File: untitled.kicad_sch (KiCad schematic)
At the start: 12 parts, among them U4 LM2596S-5, U5 LM2596S-12

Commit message: add last footprints
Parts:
- C1, C6: value CP -> 470uF; footprint Capacitor_THT:CP_Radial_D10.0mm_P5.00mm -> Capacitor_THT:CP_Radial_D12.5mm_P5.00mm
- C2, C7: value CP -> 220uF
- L1, L2, L3, L4: value L -> 10uH
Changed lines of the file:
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@@
       (effects (font (size 1.27 1.27)) (justify left))
     )
-    (property "Value" "CP" (id 1) (at 58.8772 54.483 0)
-      (effects (font (size 1.27 1.27)) (justify left))
-    )
-    (property "Footprint" "Capacitor_THT:CP_Radial_D10.0mm_P5.00mm" (id 2) (at 56.8452 57.15 0)
+    (property "Value" "470uF" (id 1) (at 58.8772 54.483 0)
+      (effects (font (size 1.27 1.27)) (justify left))
+    )
+    (property "Footprint" "Capacitor_THT:CP_Radial_D12.5mm_P5.00mm" (id 2) (at 56.8452 57.15 0)
       (effects (font (size 1.27 1.27)) hide)
     )
@@
     (in_bom yes) (on_board yes)
     (property "Reference" "L3" (id 0) (at 129.54 42.3926 90))
-    (property "Value" "L" (id 1) (at 129.54 44.704 90))
+    (property "Value" "10uH" (id 1) (at 129.54 44.704 90))
     (property "Footprint" "Inductor_SMD:L_TDK_SLF10145" (id 2) (at 129.54 46.99 0)
       (effects (font (size 1.27 1.27)) hide)
@@
       (effects (font (size 1.27 1.27)) (justify left))
     )
-    (property "Value" "CP" (id 1) (at 166.8272 57.023 0)
-      (effects (font (size 1.27 1.27)) (justify left))
-    )
-    (property "Footprint" "Capacitor_THT:CP_Radial_D10.0mm_P5.00mm" (id 2) (at 164.7952 59.69 0)
+    (property "Value" "470uF" (id 1) (at 166.8272 57.023 0)
+      (effects (font (size 1.27 1.27)) (justify left))
+    )
+    (property "Footprint" "Capacitor_THT:CP_Radial_D12.5mm_P5.00mm" (id 2) (at 164.7952 59.69 0)
       (effects (font (size 1.27 1.27)) hide)
     )
@@
       (effects (font (size 1.27 1.27)) (justify left))
     )
-    (property "Value" "CP" (id 1) (at 141.4272 54.483 0)
+    (property "Value" "220uF" (id 1) (at 141.4272 54.483 0)
       (effects (font (size 1.27 1.27)) (justify left))
     )
@@
     (in_bom yes) (on_board yes)
     (property "Reference" "L4" (id 0) (at 217.17 44.9326 90))
-    (property "Value" "L" (id 1) (at 217.17 47.244 90))
+    (property "Value" "10uH" (id 1) (at 217.17 47.244 90))
     (property "Footprint" "Inductor_SMD:L_TDK_SLF10145" (id 2) (at 217.17 49.53 0)
       (effects (font (size 1.27 1.27)) hide)
@@
       (effects (font (size 1.27 1.27)) (justify left))
     )
-    (property "Value" "CP" (id 1) (at 231.5972 57.023 0)
+    (property "Value" "220uF" (id 1) (at 231.5972 57.023 0)
       (effects (font (size 1.27 1.27)) (justify left))
     )
@@
     (in_bom yes) (on_board yes)
     (property "Reference" "L2" (id 0) (at 119.38 42.3926 90))
-    (property "Value" "L" (id 1) (at 119.38 44.704 90))
+    (property "Value" "10uH" (id 1) (at 119.38 44.704 90))
     (property "Footprint" "Inductor_SMD:L_TDK_SLF10145" (id 2) (at 119.38 46.99 0)
       (effects (font (size 1.27 1.27)) hide)
@@
     (in_bom yes) (on_board yes)
     (property "Reference" "L1" (id 0) (at 109.22 42.3926 90))
-    (property "Value" "L" (id 1) (at 109.22 44.704 90))
+    (property "Value" "10uH" (id 1) (at 109.22 44.704 90))
     (property "Footprint" "Inductor_SMD:L_TDK_SLF10145" (id 2) (at 109.22 46.99 0)
       (effects (font (size 1.27 1.27)) hide)

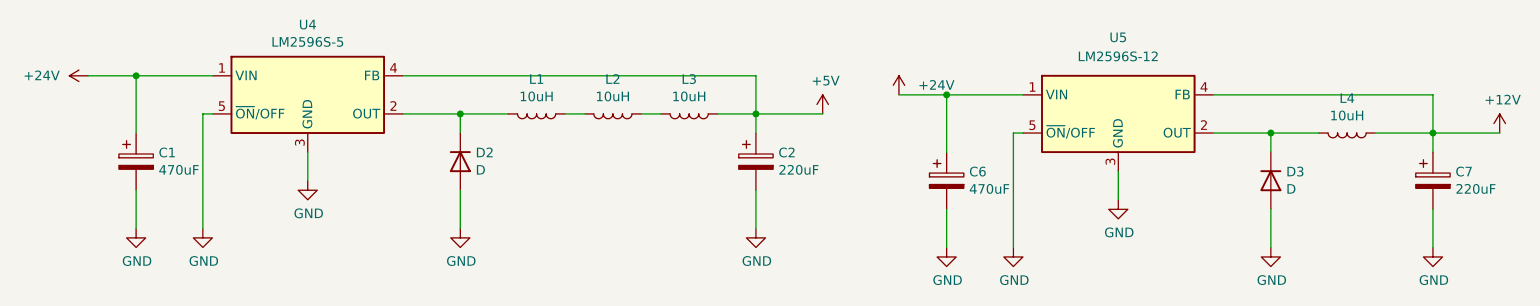
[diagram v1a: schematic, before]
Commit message: update component names
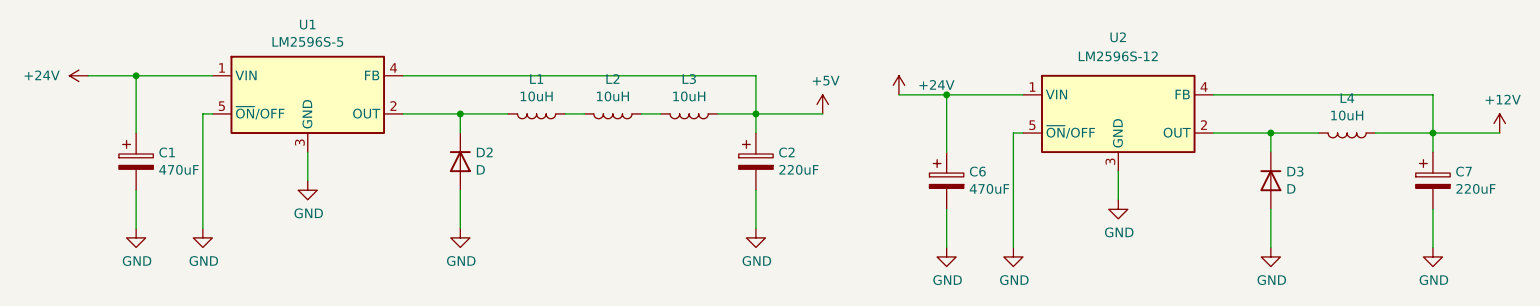
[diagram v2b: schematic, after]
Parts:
- renumbered U4 to U1, U5 to U2
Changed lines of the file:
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@@
   (symbol (lib_id "Regulator_Switching:LM2596S-5") (at 78.74 44.45 0) (unit 1)
     (in_bom yes) (on_board yes)
-    (property "Reference" "U4" (id 0) (at 78.74 35.1282 0))
+    (property "Reference" "U1" (id 0) (at 78.74 35.1282 0))
     (property "Value" "LM2596S-5" (id 1) (at 78.74 37.4396 0))
     (property "Footprint" "Package_TO_SOT_SMD:TO-263-5_TabPin3" (id 2) (at 80.01 50.8 0)
@@
   (symbol (lib_id "Regulator_Switching:LM2596S-12") (at 186.69 46.99 0) (unit 1)
     (in_bom yes) (on_board yes) (fields_autoplaced)
-    (property "Reference" "U5" (id 0) (at 186.69 36.83 0))
+    (property "Reference" "U2" (id 0) (at 186.69 36.83 0))
     (property "Value" "LM2596S-12" (id 1) (at 186.69 39.37 0))
     (property "Footprint" "Package_TO_SOT_SMD:TO-263-5_TabPin3" (id 2) (at 187.96 53.34 0)

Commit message: Elements changed and routing
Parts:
- removed L2, L3: 10uH, Inductor_SMD:L_TDK_SLF10145, symbol Device:L
- C1, C6: value 470uF -> 100uF
- C2, C7: value 220uF -> 1000uF
- D2, D3: value D -> 1N5822
- L1: value 10uH -> 100uH
- L4: value 10uH -> 100uF
- U1: value LM2596S-5 -> LM2576-05
- U2: value LM2596S-12 -> LM2576-12
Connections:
- net +5V: now also L1.1
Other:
- moved on the sheet: C2
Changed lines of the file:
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@@
 (kicad_sch (version 20211123) (generator eeschema)
   (paper "A4")
-  (junction (at 138.43 46.99) (diameter 0) (color 0 0 0 0)
-  )
   (junction (at 228.6 49.53) (diameter 0) (color 0 0 0 0)
   )
@@
   (junction (at 99.06 46.99) (diameter 0) (color 0 0 0 0)
   )
-  (wire (pts (xy 138.43 46.99) (xy 147.32 46.99))
-    (stroke (width 0) (type default) (color 0 0 0 0))
+  (junction (at 119.38 46.99) (diameter 0) (color 0 0 0 0)
   )
   (wire (pts (xy 228.6 49.53) (xy 228.6 52.07))
     (stroke (width 0) (type default) (color 0 0 0 0))
   )
-  (wire (pts (xy 115.57 46.99) (xy 113.03 46.99))
+  (wire (pts (xy 113.03 46.99) (xy 119.38 46.99))
     (stroke (width 0) (type default) (color 0 0 0 0))
   )
@@
     (stroke (width 0) (type default) (color 0 0 0 0))
   )
-  (wire (pts (xy 125.73 46.99) (xy 123.19 46.99))
-    (stroke (width 0) (type default) (color 0 0 0 0))
-  )
   (wire (pts (xy 228.6 59.69) (xy 228.6 64.77))
     (stroke (width 0) (type default) (color 0 0 0 0))
@@
     (stroke (width 0) (type default) (color 0 0 0 0))
   )
+  (wire (pts (xy 119.38 54.61) (xy 119.38 62.23))
+    (stroke (width 0) (type default) (color 0 0 0 0))
+  )
   (wire (pts (xy 207.01 49.53) (xy 207.01 52.07))
     (stroke (width 0) (type default) (color 0 0 0 0))
   )
-  (wire (pts (xy 138.43 57.15) (xy 138.43 62.23))
-    (stroke (width 0) (type default) (color 0 0 0 0))
-  )
   (wire (pts (xy 163.83 44.45) (xy 157.48 44.45))
     (stroke (width 0) (type default) (color 0 0 0 0))
@@
     (stroke (width 0) (type default) (color 0 0 0 0))
   )
-  (wire (pts (xy 133.35 46.99) (xy 138.43 46.99))
+  (wire (pts (xy 119.38 46.99) (xy 129.54 46.99))
     (stroke (width 0) (type default) (color 0 0 0 0))
   )
@@
     (stroke (width 0) (type default) (color 0 0 0 0))
   )
+  (wire (pts (xy 91.44 41.91) (xy 119.38 41.91))
+    (stroke (width 0) (type default) (color 0 0 0 0))
+  )
   (wire (pts (xy 207.01 64.77) (xy 207.01 59.69))
     (stroke (width 0) (type default) (color 0 0 0 0))
@@
     (stroke (width 0) (type default) (color 0 0 0 0))
   )
-  (wire (pts (xy 138.43 41.91) (xy 138.43 46.99))
-    (stroke (width 0) (type default) (color 0 0 0 0))
-  )
-  (wire (pts (xy 138.43 46.99) (xy 138.43 49.53))
-    (stroke (width 0) (type default) (color 0 0 0 0))
-  )
   (wire (pts (xy 163.83 44.45) (xy 163.83 52.07))
     (stroke (width 0) (type default) (color 0 0 0 0))
@@
     (stroke (width 0) (type default) (color 0 0 0 0))
   )
+  (wire (pts (xy 119.38 41.91) (xy 119.38 46.99))
+    (stroke (width 0) (type default) (color 0 0 0 0))
+  )
   (wire (pts (xy 91.44 46.99) (xy 99.06 46.99))
     (stroke (width 0) (type default) (color 0 0 0 0))
@@
   )
   (wire (pts (xy 199.39 49.53) (xy 207.01 49.53))
-    (stroke (width 0) (type default) (color 0 0 0 0))
-  )
-  (wire (pts (xy 91.44 41.91) (xy 138.43 41.91))
     (stroke (width 0) (type default) (color 0 0 0 0))
   )
@@
       (effects (font (size 1.27 1.27)) (justify left))
     )
-    (property "Value" "470uF" (id 1) (at 58.8772 54.483 0)
+    (property "Value" "100uF" (id 1) (at 58.8772 54.483 0)
       (effects (font (size 1.27 1.27)) (justify left))
     )
@@
     (in_bom yes) (on_board yes)
     (property "Reference" "U1" (id 0) (at 78.74 35.1282 0))
-    (property "Value" "LM2596S-5" (id 1) (at 78.74 37.4396 0))
+    (property "Value" "LM2576-05" (id 1) (at 78.74 37.4396 0))
     (property "Footprint" "Package_TO_SOT_SMD:TO-263-5_TabPin3" (id 2) (at 80.01 50.8 0)
       (effects (font (size 1.27 1.27) italic) (justify left) hide)
@@
     (pin "5")
   )
-  (symbol (lib_id "Device:L") (at 129.54 46.99 270) (unit 1)
-    (in_bom yes) (on_board yes)
-    (property "Reference" "L3" (id 0) (at 129.54 42.3926 90))
-    (property "Value" "10uH" (id 1) (at 129.54 44.704 90))
-    (property "Footprint" "Inductor_SMD:L_TDK_SLF10145" (id 2) (at 129.54 46.99 0)
-      (effects (font (size 1.27 1.27)) hide)
-    )
-    (property "Datasheet" "~" (id 3) (at 129.54 46.99 0)
-      (effects (font (size 1.27 1.27)) hide)
-    )
-    (pin "1")
-    (pin "2")
-  )
   (symbol (lib_id "power:GND") (at 78.74 55.88 0) (unit 1)
     (in_bom yes) (on_board yes)
@@
       (effects (font (size 1.27 1.27)) (justify left))
     )
-    (property "Value" "470uF" (id 1) (at 166.8272 57.023 0)
+    (property "Value" "100uF" (id 1) (at 166.37 58.42 0)
       (effects (font (size 1.27 1.27)) (justify left))
     )
@@
     (pin "1")
   )
-  (symbol (lib_id "power:GND") (at 138.43 62.23 0) (unit 1)
-    (in_bom yes) (on_board yes)
-    (property "Reference" "#PWR0125" (id 0) (at 138.43 68.58 0)
-      (effects (font (size 1.27 1.27)) hide)
-    )
-    (property "Value" "GND" (id 1) (at 138.557 66.6242 0))
-    (property "Footprint" "" (id 2) (at 138.43 62.23 0)
-      (effects (font (size 1.27 1.27)) hide)
-    )
-    (property "Datasheet" "" (id 3) (at 138.43 62.23 0)
+  (symbol (lib_id "power:GND") (at 119.38 62.23 0) (unit 1)
+    (in_bom yes) (on_board yes)
+    (property "Reference" "#PWR0125" (id 0) (at 119.38 68.58 0)
+      (effects (font (size 1.27 1.27)) hide)
+    )
+    (property "Value" "GND" (id 1) (at 119.507 66.6242 0))
+    (property "Footprint" "" (id 2) (at 119.38 62.23 0)
+      (effects (font (size 1.27 1.27)) hide)
+    )
+    (property "Datasheet" "" (id 3) (at 119.38 62.23 0)
       (effects (font (size 1.27 1.27)) hide)
     )
@@
     (pin "1")
   )
-  (symbol (lib_id "Device:CP") (at 138.43 53.34 0) (unit 1)
-    (in_bom yes) (on_board yes)
-    (property "Reference" "C2" (id 0) (at 141.4272 52.1716 0)
-      (effects (font (size 1.27 1.27)) (justify left))
-    )
-    (property "Value" "220uF" (id 1) (at 141.4272 54.483 0)
-      (effects (font (size 1.27 1.27)) (justify left))
-    )
-    (property "Footprint" "Capacitor_THT:CP_Radial_D8.0mm_P3.50mm" (id 2) (at 139.3952 57.15 0)
-      (effects (font (size 1.27 1.27)) hide)
-    )
-    (property "Datasheet" "~" (id 3) (at 138.43 53.34 0)
+  (symbol (lib_id "Device:CP") (at 119.38 50.8 0) (unit 1)
+    (in_bom yes) (on_board yes)
+    (property "Reference" "C2" (id 0) (at 122.3772 49.6316 0)
+      (effects (font (size 1.27 1.27)) (justify left))
+    )
+    (property "Value" "1000uF" (id 1) (at 122.3772 51.943 0)
+      (effects (font (size 1.27 1.27)) (justify left))
+    )
+    (property "Footprint" "Capacitor_THT:CP_Radial_D8.0mm_P3.50mm" (id 2) (at 120.3452 54.61 0)
+      (effects (font (size 1.27 1.27)) hide)
+    )
+    (property "Datasheet" "~" (id 3) (at 119.38 50.8 0)
       (effects (font (size 1.27 1.27)) hide)
     )
@@
     (in_bom yes) (on_board yes) (fields_autoplaced)
     (property "Reference" "U2" (id 0) (at 186.69 36.83 0))
-    (property "Value" "LM2596S-12" (id 1) (at 186.69 39.37 0))
+    (property "Value" "LM2576-12" (id 1) (at 186.69 39.37 0))
     (property "Footprint" "Package_TO_SOT_SMD:TO-263-5_TabPin3" (id 2) (at 187.96 53.34 0)
       (effects (font (size 1.27 1.27) italic) (justify left) hide)
@@
     (in_bom yes) (on_board yes)
     (property "Reference" "L4" (id 0) (at 217.17 44.9326 90))
-    (property "Value" "10uH" (id 1) (at 217.17 47.244 90))
+    (property "Value" "100uF" (id 1) (at 217.17 47.244 90))
     (property "Footprint" "Inductor_SMD:L_TDK_SLF10145" (id 2) (at 217.17 49.53 0)
       (effects (font (size 1.27 1.27)) hide)
@@
       (effects (font (size 1.27 1.27)) (justify left))
     )
-    (property "Value" "D" (id 1) (at 209.042 57.023 90)
+    (property "Value" "1N5822" (id 1) (at 209.042 57.023 90)
       (effects (font (size 1.27 1.27)) (justify left))
     )
@@
       (effects (font (size 1.27 1.27)) (justify left))
     )
-    (property "Value" "220uF" (id 1) (at 231.5972 57.023 0)
+    (property "Value" "1000uF" (id 1) (at 231.5972 57.023 0)
       (effects (font (size 1.27 1.27)) (justify left))
     )
@@
     (pin "2")
   )
-  (symbol (lib_id "Device:L") (at 119.38 46.99 270) (unit 1)
-    (in_bom yes) (on_board yes)
-    (property "Reference" "L2" (id 0) (at 119.38 42.3926 90))
-    (property "Value" "10uH" (id 1) (at 119.38 44.704 90))
-    (property "Footprint" "Inductor_SMD:L_TDK_SLF10145" (id 2) (at 119.38 46.99 0)
-      (effects (font (size 1.27 1.27)) hide)
-    )
-    (property "Datasheet" "~" (id 3) (at 119.38 46.99 0)
-      (effects (font (size 1.27 1.27)) hide)
-    )
-    (pin "1")
-    (pin "2")
-  )
   (symbol (lib_id "Device:L") (at 109.22 46.99 270) (unit 1)
     (in_bom yes) (on_board yes)
     (property "Reference" "L1" (id 0) (at 109.22 42.3926 90))
-    (property "Value" "10uH" (id 1) (at 109.22 44.704 90))
+    (property "Value" "100uH" (id 1) (at 109.22 44.704 90))
     (property "Footprint" "Inductor_SMD:L_TDK_SLF10145" (id 2) (at 109.22 46.99 0)
       (effects (font (size 1.27 1.27)) hide)
@@
       (effects (font (size 1.27 1.27)) (justify left))
     )
-    (property "Value" "D" (id 1) (at 101.092 54.483 90)
+    (property "Value" "1N5822" (id 1) (at 101.092 54.483 90)
       (effects (font (size 1.27 1.27)) (justify left))
     )
@@
     (pin "2")
   )
-  (symbol (lib_id "power:+5V") (at 147.32 46.99 0) (unit 1)
-    (in_bom yes) (on_board yes)
-    (property "Reference" "#PWR0127" (id 0) (at 147.32 50.8 0)
-      (effects (font (size 1.27 1.27)) hide)
-    )
-    (property "Value" "+5V" (id 1) (at 147.701 42.5958 0))
-    (property "Footprint" "" (id 2) (at 147.32 46.99 0)
-      (effects (font (size 1.27 1.27)) hide)
-    )
-    (property "Datasheet" "" (id 3) (at 147.32 46.99 0)
-      (effects (font (size 1.27 1.27)) hide)
-    )
+  (symbol (lib_id "power:+5V") (at 129.54 46.99 0) (unit 1)
+    (in_bom yes) (on_board yes)
+    (property "Reference" "#PWR0127" (id 0) (at 129.54 50.8 0)
+      (effects (font (size 1.27 1.27)) hide)
+    )
+    (property "Value" "+5V" (id 1) (at 129.921 42.5958 0))
+    (property "Footprint" "" (id 2) (at 129.54 46.99 0)
+      (effects (font (size 1.27 1.27)) hide)
+    )
+    (property "Datasheet" "" (id 3) (at 129.54 46.99 0)
+      (effects (font (size 1.27 1.27)) hide)
+    )
